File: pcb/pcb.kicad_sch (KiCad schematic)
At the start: 21 parts, among them J1 USB_C_Receptacle_USB2.0_14P, U1 RP2040, U2 NCP1117-3.3_SOT223

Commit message: logging off for the night - completed the schematic
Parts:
- added C15, C16: 33pF, Capacitor_SMD:C_0402_1005Metric, symbol Device:C
- added C17: 0.1uF, Capacitor_SMD:C_0402_1005Metric, symbol Device:C
- added J2, J3: Conn_01x20, Connector_PinHeader_2.54mm:PinHeader_1x20_P2.54mm_Vertical, symbol Connector_Generic:Conn_01x20
- added J4: Conn_01x03, Connector_PinHeader_2.54mm:PinHeader_1x03_P2.54mm_Vertical, symbol Connector_Generic:Conn_01x03
- added R5, R6: 1k, Resistor_SMD:R_0402_1005Metric, symbol Device:R
- added R7: 10k, Resistor_SMD:R_0402_1005Metric, symbol Device:R
- added SW1: SW_Push, Button_Switch_SMD:SW_Push_SPST_NO_Alps_SKRK, symbol Switch:SW_Push
- added U3: W25Q128JVS, Package_SO:SOIC-8_5.3x5.3mm_P1.27mm, symbol Memory_Flash:W25Q128JVS
- added Y1: 12 MHz, Crystal:Crystal_SMD_3225-4Pin_3.2x2.5mm, symbol Device:Crystal_GND24
- C1, C10, C11, C12, C13, C14, C2, C3, C4, C5, C6, C7, C8, C9: footprint (none) -> Capacitor_SMD:C_0402_1005Metric
- J1: footprint (none) -> Connector_USB:USB_C_Receptacle_HRO_TYPE-C-31-M-12
- R1, R2, R3, R4: footprint (none) -> Resistor_SMD:R_0402_1005Metric
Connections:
- net +3V3: now also C17.1, J3.5 (Pin_5), R7.1, U3.8 (VCC)
- net GND: now also U1.19 (TESTEN), C15.1, C16.1, C17.2, J2.13 (Pin_13), J2.18 (Pin_18), J2.3 (Pin_3), J2.8 (Pin_8), J3.13 (Pin_13), J3.18 (Pin_18), J3.3 (Pin_3), J3.8 (Pin_8), J4.2 (Pin_2), SW1.1, U3.4 (GND), Y1.2, Y1.4
- net VBUS: now also J3.1 (Pin_1)
- net GPIO8: now reaches U1.11 (GPIO8)
- net GPIO8: now also J2.11 (Pin_11)
- net GPIO9: now reaches U1.12 (GPIO9)
- net GPIO9: now also J2.12 (Pin_12)
- net GPIO10: now reaches U1.13 (GPIO10)
- net GPIO10: now also J2.14 (Pin_14)
- net GPIO11: now reaches U1.14 (GPIO11)
- net GPIO11: now also J2.15 (Pin_15)
- net GPIO12: now reaches U1.15 (GPIO12)
- net GPIO12: now also J2.16 (Pin_16)
- net GPIO13: now reaches U1.16 (GPIO13)
- net GPIO13: now also J2.17 (Pin_17)
- net GPIO14: now reaches U1.17 (GPIO14)
- net GPIO14: now also J2.19 (Pin_19)
- net GPIO15: now reaches U1.18 (GPIO15)
- net GPIO15: now also J2.20 (Pin_20)
- net GPIO0: now reaches U1.2 (GPIO0)
- net GPIO0: now also J2.1 (Pin_1)
- net XIN: now reaches U1.20 (XIN)
- net XIN: now also C16.2, Y1.3
- net XOUT: now reaches U1.21 (XOUT)
- net XOUT: now also R5.2
- net SWCLK: now reaches U1.24 (SWCLK)
- net SWCLK: now also J4.1 (Pin_1)
- net SWD: now reaches U1.25 (SWD)
- net SWD: now also J4.3 (Pin_3)
- net RUN: now reaches U1.26 (RUN)
- net RUN: now also J3.11 (Pin_11)
- net GPIO16: now reaches U1.27 (GPIO16)
- net GPIO16: now also J3.20 (Pin_20)
- net GPIO17: now reaches U1.28 (GPIO17)
- net GPIO17: now also J3.19 (Pin_19)
- net GPIO18: now reaches U1.29 (GPIO18)
- net GPIO18: now also J3.17 (Pin_17)
- net GPIO1: now reaches U1.3 (GPIO1)
- net GPIO1: now also J2.2 (Pin_2)
- net GPIO19: now reaches U1.30 (GPIO19)
- net GPIO19: now also J3.16 (Pin_16)
- net GPIO20: now reaches U1.31 (GPIO20)
- net GPIO20: now also J3.15 (Pin_15)
- net GPIO21: now reaches U1.32 (GPIO21)
- net GPIO21: now also J3.14 (Pin_14)
- net GPIO22: now reaches U1.34 (GPIO22)
- net GPIO22: now also J3.12 (Pin_12)
- net GPIO23: now reaches U1.35 (GPIO23)
- net GPIO23: now also J3.10 (Pin_10)
- net GPIO24: now reaches U1.36 (GPIO24)
- net GPIO24: now also J3.9 (Pin_9)
- net GPIO26_ADC0: now reaches U1.38 (GPIO26_ADC0)
- net GPIO26_ADC0: now also J3.7 (Pin_7)
- net GPIO27_ADC1: now reaches U1.39 (GPIO27_ADC1)
- net GPIO27_ADC1: now also J3.6 (Pin_6)
- net GPIO2: now reaches U1.4 (GPIO2)
- net GPIO2: now also J2.4 (Pin_4)
- net GPIO28_ADC2: now reaches U1.40 (GPIO28_ADC2)
- net GPIO28_ADC2: now also J3.4 (Pin_4)
- net GPIO29_ADC3: now reaches U1.41 (GPIO29_ADC3)
- net GPIO29_ADC3: now also J3.2 (Pin_2)
- net GPIO3: now reaches U1.5 (GPIO3)
- net GPIO3: now also J2.5 (Pin_5)
- net QSPI_SD3: now reaches U1.51 (QSPI_SD3)
- net QSPI_SD3: now also U3.7 (~{HOLD}/~{RESET}/IO_{3})
- net QSPI_SCLK: now reaches U1.52 (QSPI_SCLK)
- net QSPI_SCLK: now also U3.6 (CLK)
- net QSPI_SD0: now reaches U1.53 (QSPI_SD0)
- net QSPI_SD0: now also U3.5 (DI/IO_{0})
- net QSPI_SD2: now reaches U1.54 (QSPI_SD2)
- net QSPI_SD2: now also U3.3 (~{WP}/IO_{2})
- net QSPI_SD1: now reaches U1.55 (QSPI_SD1)
- net QSPI_SD1: now also U3.2 (DO/IO_{1})
- net QSPI_SS: now reaches U1.56 (QSPI_SS)
- net QSPI_SS: now also R6.2, R7.2, U3.1 (~{CS})
- net GPIO4: now reaches U1.6 (GPIO4)
- net GPIO4: now also J2.6 (Pin_6)
- net GPIO5: now reaches U1.7 (GPIO5)
- net GPIO5: now also J2.7 (Pin_7)
- net GPIO6: now reaches U1.8 (GPIO6)
- net GPIO6: now also J2.9 (Pin_9)
- net GPIO7: now reaches U1.9 (GPIO7)
- net GPIO7: now also J2.10 (Pin_10)
- new net: R6.1, SW1.2
- new net: C15.2, R5.1, Y1.1
- no-connect marks 0 -> 1
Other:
- moved on the sheet: C1, C13, C14, C2, C3, C4, C5, C6, C7, C8, C9, J1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

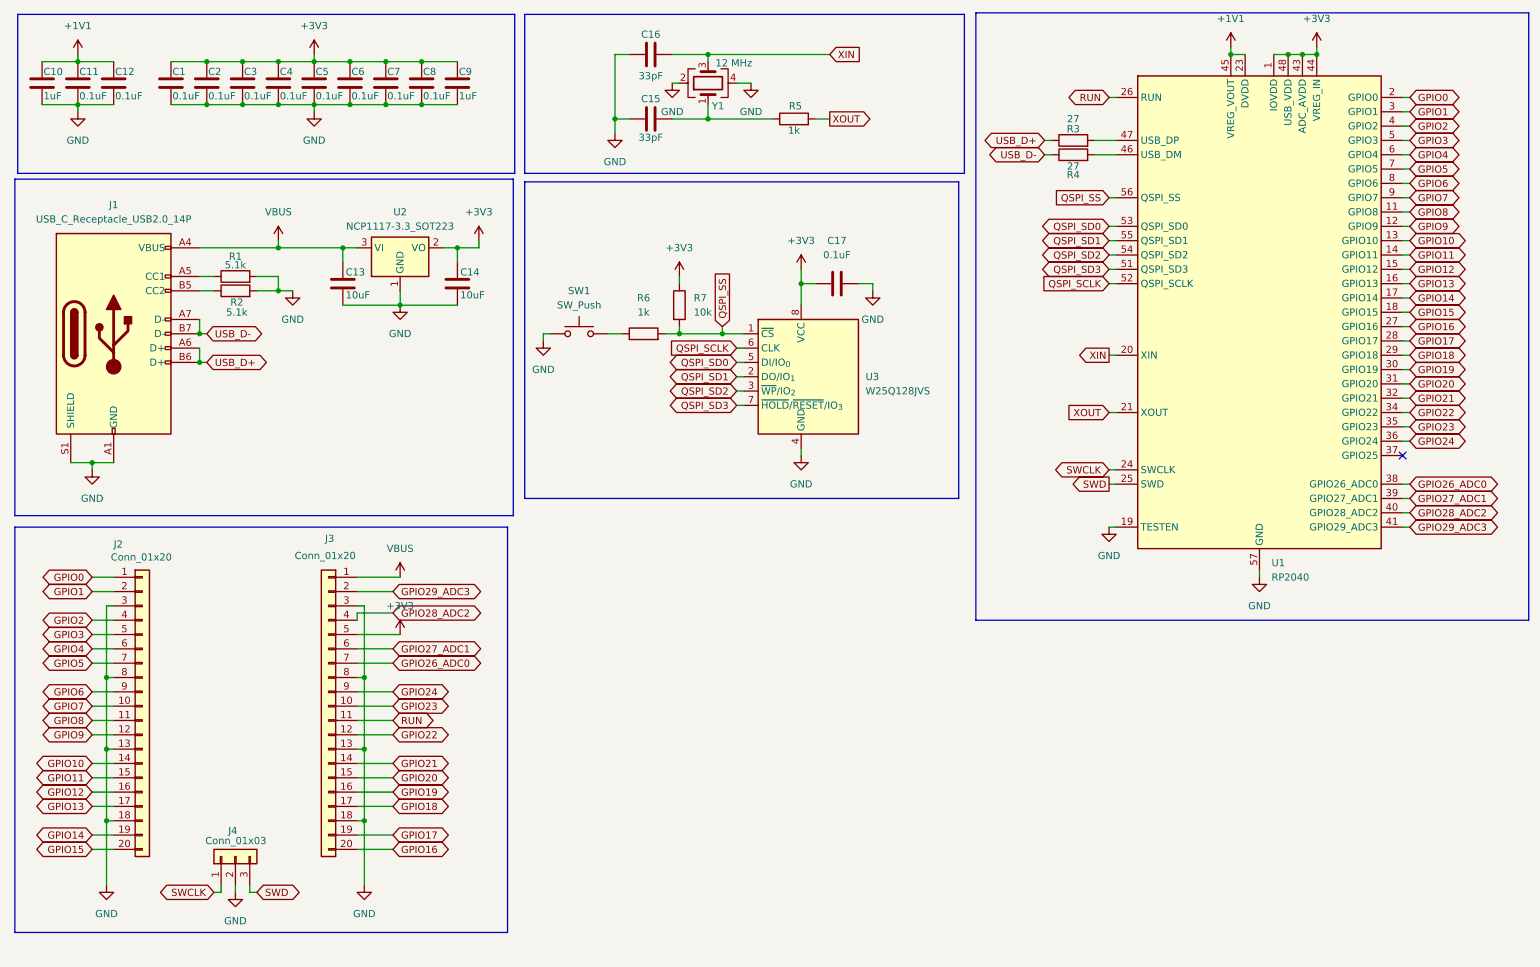
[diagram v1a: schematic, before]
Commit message: feat: added the neopixel status led
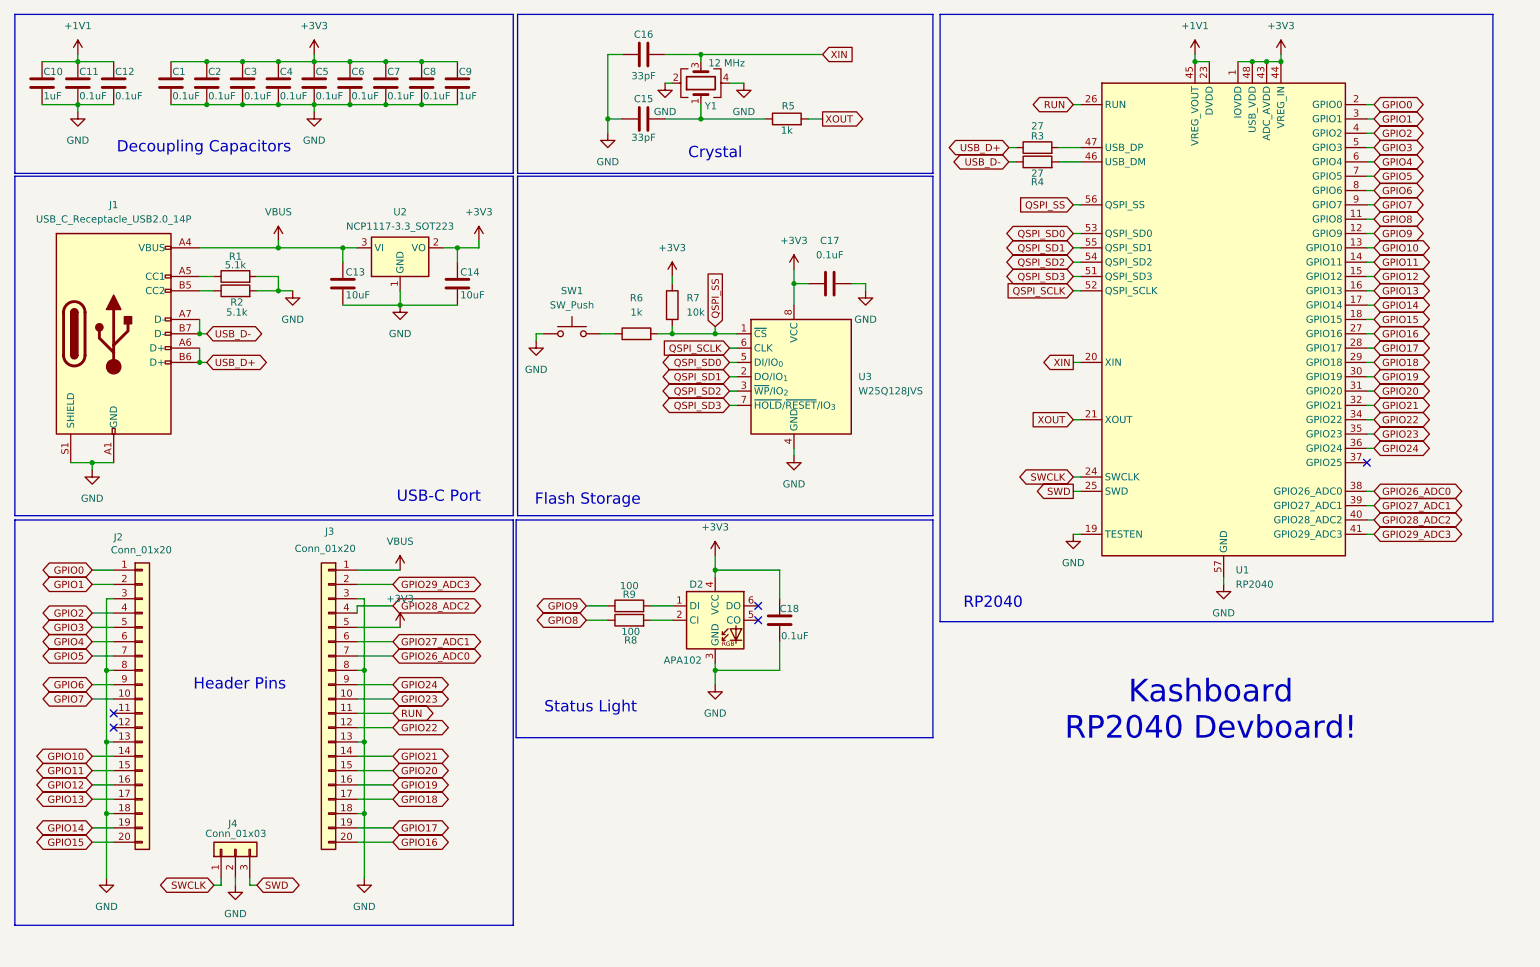
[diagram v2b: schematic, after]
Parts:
- added C18: 0.1uF, symbol Device:C
- added D2: APA102, LED_SMD:LED_RGB_5050-6, symbol LED:APA102
- added R8, R9: 100, symbol Device:R
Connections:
- net +3V3: now also C18.1, D2.4 (VCC)
- net GND: now also C18.2, D2.3 (GND)
- net GPIO8: now also R8.1; no longer J2.11 (Pin_11)
- net GPIO9: now also R9.1; no longer J2.12 (Pin_12)
- new net: D2.1 (DI), R9.2
- new net: D2.2 (CI), R8.2
- no-connect marks 1 -> 5
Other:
- note added: "Crystal"
- note added: "Decoupling Capacitors"
- note added: "Flash Storage"
- note added: "Header Pins"
- note added: "Kashboard RP2040 Devboard!"
- note added: "RP2040"
- note added: "Status Light"
- note added: "USB-C Port"
- moved on the sheet: C15, C16, C17, J2, J3, J4, R3, R4, R5, R6, R7, SW1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

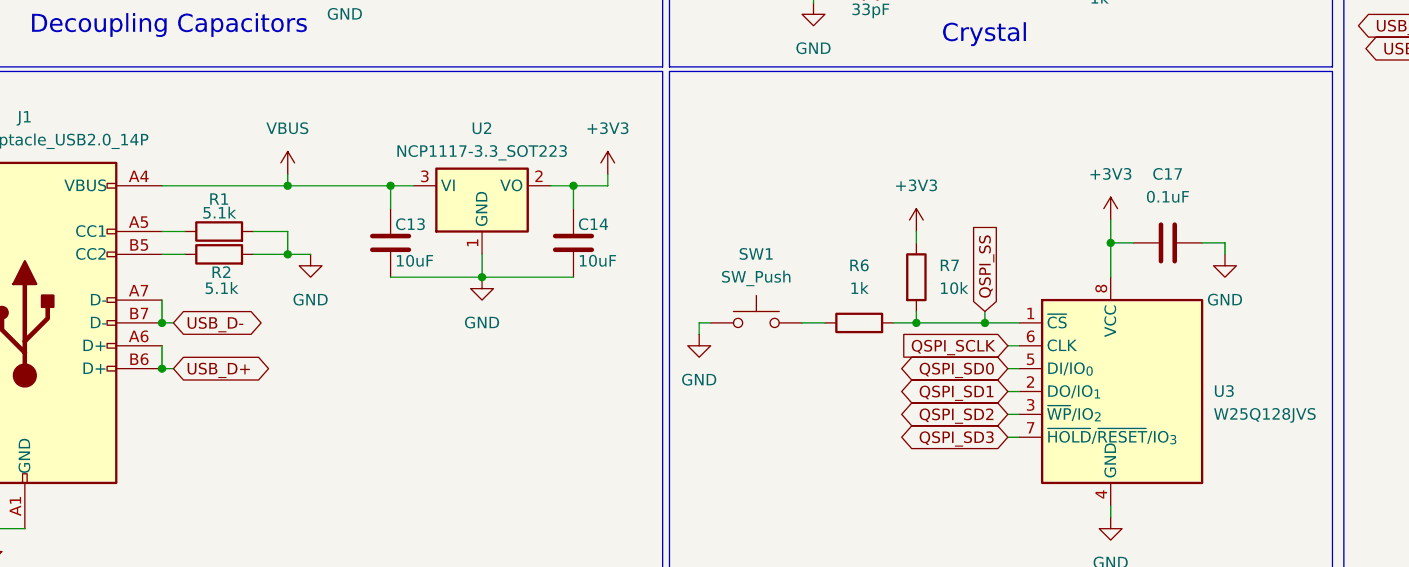
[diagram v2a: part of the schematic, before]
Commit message: updated the schematic with better formatting
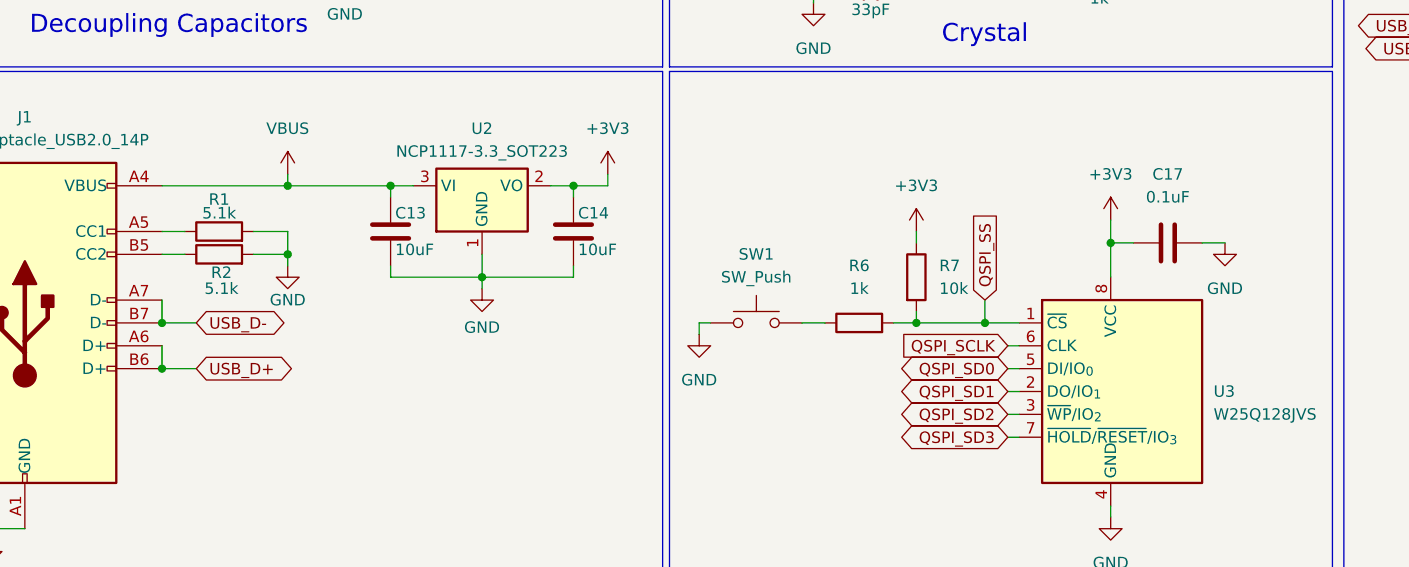
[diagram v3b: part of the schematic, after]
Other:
- moved on the sheet: C13, C14
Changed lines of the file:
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@@
 	(wire
 		(pts
-			(xy 165.1 62.23) (xy 165.1 63.5)
-		)
-		(stroke
-			(width 0)
-			(type default)
-		)
-	)
-	(wire
-		(pts
 			(xy 254 63.5) (xy 255.27 63.5)
 		)
@@
 	(wire
 		(pts
+			(xy 82.55 63.5) (xy 82.55 66.04)
+		)
+		(stroke
+			(width 0)
+			(type default)
+		)
+	)
+	(wire
+		(pts
 			(xy 73.66 30.48) (xy 80.01 30.48)
 		)
@@
 	(wire
 		(pts
-			(xy 72.39 55.88) (xy 72.39 58.42)
+			(xy 72.39 55.88) (xy 72.39 57.15)
 		)
 		(stroke
@@
 	(wire
 		(pts
-			(xy 138.43 69.85) (xy 138.43 71.12)
+			(xy 138.43 68.58) (xy 138.43 71.12)
 		)
 		(stroke
@@
 	(wire
 		(pts
-			(xy 46.99 71.12) (xy 48.26 71.12)
+			(xy 46.99 71.12) (xy 50.8 71.12)
 		)
 		(stroke
@@
 	(wire
 		(pts
-			(xy 82.55 63.5) (xy 82.55 66.04)
+			(xy 201.93 76.2) (xy 203.2 76.2)
 		)
 		(stroke
@@
 	(wire
 		(pts
-			(xy 201.93 76.2) (xy 203.2 76.2)
+			(xy 80.01 30.48) (xy 86.36 30.48)
 		)
 		(stroke
@@
 	(wire
 		(pts
-			(xy 80.01 30.48) (xy 86.36 30.48)
+			(xy 254 43.18) (xy 255.27 43.18)
 		)
 		(stroke
@@
 	(wire
 		(pts
-			(xy 254 43.18) (xy 255.27 43.18)
+			(xy 72.39 66.04) (xy 72.39 64.77)
 		)
 		(stroke
@@
 	(wire
 		(pts
-			(xy 60.96 63.5) (xy 63.5 63.5)
-		)
-		(stroke
-			(width 0)
-			(type default)
-		)
-	)
-	(wire
-		(pts
 			(xy 199.39 38.1) (xy 203.2 38.1)
 		)
@@
 	(wire
 		(pts
-			(xy 92.71 55.88) (xy 92.71 58.42)
+			(xy 92.71 55.88) (xy 92.71 57.15)
 		)
 		(stroke
@@
 	(wire
 		(pts
-			(xy 46.99 76.2) (xy 48.26 76.2)
+			(xy 46.99 76.2) (xy 50.8 76.2)
 		)
 		(stroke
@@
 	(wire
 		(pts
+			(xy 92.71 66.04) (xy 92.71 64.77)
+		)
+		(stroke
+			(width 0)
+			(type default)
+		)
+	)
+	(wire
+		(pts
 			(xy 135.89 21.59) (xy 135.89 22.86)
 		)
@@
 	(wire
 		(pts
+			(xy 60.96 64.77) (xy 60.96 63.5)
+		)
+		(stroke
+			(width 0)
+			(type default)
+		)
+	)
+	(wire
+		(pts
 			(xy 201.93 99.06) (xy 203.2 99.06)
 		)
@@
 	(wire
 		(pts
+			(xy 82.55 67.31) (xy 82.55 66.04)
+		)
+		(stroke
+			(width 0)
+			(type default)
+		)
+	)
+	(wire
+		(pts
 			(xy 27.94 158.75) (xy 31.75 158.75)
 		)
@@
 	(global_label "QSPI_SS"
 		(shape input)
-		(at 138.43 69.85 90)
+		(at 138.43 68.58 90)
 		(fields_autoplaced yes)
 		(effects
@@
 		)
 		(property "Intersheetrefs" "${INTERSHEET_REFS}"
-			(at 138.43 59.0634 90)
+			(at 138.43 57.7934 90)
 			(effects
 				(font
@@
 	(global_label "USB_D-"
 		(shape bidirectional)
-		(at 48.26 71.12 0)
+		(at 50.8 71.12 0)
 		(fields_autoplaced yes)
 		(effects
@@
 		)
 		(property "Intersheetrefs" "${INTERSHEET_REFS}"
-			(at 59.9765 71.12 0)
+			(at 62.5165 71.12 0)
 			(effects
 				(font
@@
 	(global_label "USB_D+"
 		(shape bidirectional)
-		(at 48.26 76.2 0)
+		(at 50.8 76.2 0)
 		(fields_autoplaced yes)
 		(effects
@@
 		)
 		(property "Intersheetrefs" "${INTERSHEET_REFS}"
-			(at 59.9765 76.2 0)
+			(at 62.5165 76.2 0)
 			(effects
 				(font
@@
 	(symbol
 		(lib_id "Device:C")
-		(at 72.39 62.23 180)
+		(at 72.39 60.96 180)
 		(unit 1)
 		(exclude_from_sim no)
@@
 		(dnp no)
 		(property "Reference" "C13"
-			(at 72.898 60.198 0)
+			(at 72.898 58.928 0)
 			(effects
 				(font
@@
 		)
 		(property "Value" "10uF"
-			(at 72.898 64.262 0)
+			(at 72.898 62.992 0)
 			(effects
 				(font
@@
 		)
 		(property "Footprint" "Capacitor_SMD:C_0402_1005Metric"
-			(at 71.4248 58.42 0)
+			(at 71.4248 57.15 0)
 			(effects
 				(font
@@
 		)
 		(property "Datasheet" "~"
-			(at 72.39 62.23 0)
+			(at 72.39 60.96 0)
 			(effects
 				(font
@@
 		)
 		(property "Description" "Unpolarized capacitor"
-			(at 72.39 62.23 0)
+			(at 72.39 60.96 0)
 			(effects
 				(font
@@
 	(symbol
 		(lib_id "power:GND")
-		(at 165.1 63.5 0)
+		(at 165.1 62.23 0)
 		(unit 1)
 		(exclude_from_sim no)
@@
 		(fields_autoplaced yes)
 		(property "Reference" "#PWR018"
-			(at 165.1 69.85 0)
+			(at 165.1 68.58 0)
 			(effects
 				(font
@@
 		)
 		(property "Value" "GND"
-			(at 165.1 68.58 0)
+			(at 165.1 67.31 0)
 			(effects
 				(font
@@
 		)
 		(property "Footprint" ""
-			(at 165.1 63.5 0)
+			(at 165.1 62.23 0)
 			(effects
 				(font
@@
 		)
 		(property "Datasheet" ""
-			(at 165.1 63.5 0)
+			(at 165.1 62.23 0)
 			(effects
 				(font
@@
 		)
 		(property "Description" "Power symbol creates a global label with name \"GND\" , ground"
-			(at 165.1 63.5 0)
+			(at 165.1 62.23 0)
 			(effects
 				(font
@@
 	(symbol
 		(lib_id "Device:C")
-		(at 92.71 62.23 180)
+		(at 92.71 60.96 180)
 		(unit 1)
 		(exclude_from_sim no)
@@
 		(dnp no)
 		(property "Reference" "C14"
-			(at 93.218 60.198 0)
+			(at 93.218 58.928 0)
 			(effects
 				(font
@@
 		)
 		(property "Value" "10uF"
-			(at 93.218 64.262 0)
+			(at 93.218 62.992 0)
 			(effects
 				(font
@@
 		)
 		(property "Footprint" "Capacitor_SMD:C_0402_1005Metric"
-			(at 91.7448 58.42 0)
+			(at 91.7448 57.15 0)
 			(effects
 				(font
@@
 		)
 		(property "Datasheet" "~"
-			(at 92.71 62.23 0)
+			(at 92.71 60.96 0)
 			(effects
 				(font
@@
 		)
 		(property "Description" "Unpolarized capacitor"
-			(at 92.71 62.23 0)
+			(at 92.71 60.96 0)
 			(effects
 				(font
@@
 	(symbol
 		(lib_id "power:GND")
-		(at 82.55 66.04 0)
+		(at 82.55 67.31 0)
 		(unit 1)
 		(exclude_from_sim no)
@@
 		(on_board yes)
 		(dnp no)
-		(fields_autoplaced yes)
 		(property "Reference" "#PWR010"
-			(at 82.55 72.39 0)
+			(at 82.55 73.66 0)
 			(effects
 				(font
@@
 		)
 		(property "Value" "GND"
-			(at 82.55 71.12 0)
+			(at 82.55 71.628 0)
 			(effects
 				(font
@@
 		)
 		(property "Footprint" ""
-			(at 82.55 66.04 0)
+			(at 82.55 67.31 0)
 			(effects
 				(font
@@
 		)
 		(property "Datasheet" ""
-			(at 82.55 66.04 0)
+			(at 82.55 67.31 0)
 			(effects
 				(font
@@
 		)
 		(property "Description" "Power symbol creates a global label with name \"GND\" , ground"
-			(at 82.55 66.04 0)
+			(at 82.55 67.31 0)
 			(effects
 				(font
@@
 	(symbol
 		(lib_id "power:GND")
-		(at 63.5 63.5 0)
+		(at 60.96 64.77 0)
 		(unit 1)
 		(exclude_from_sim no)
@@
 		(on_board yes)
 		(dnp no)
-		(fields_autoplaced yes)
 		(property "Reference" "#PWR09"
-			(at 63.5 69.85 0)
+			(at 60.96 71.12 0)
 			(effects
 				(font
@@
 		)
 		(property "Value" "GND"
-			(at 63.5 68.58 0)
+			(at 60.96 68.58 0)
 			(effects
 				(font
@@
 		)
 		(property "Footprint" ""
-			(at 63.5 63.5 0)
+			(at 60.96 64.77 0)
 			(effects
 				(font
@@
 		)
 		(property "Datasheet" ""
-			(at 63.5 63.5 0)
+			(at 60.96 64.77 0)
 			(effects
 				(font
@@
 		)
 		(property "Description" "Power symbol creates a global label with name \"GND\" , ground"
-			(at 63.5 63.5 0)
+			(at 60.96 64.77 0)
 			(effects
 				(font

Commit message: feat: updated most of the pcb, still have some capacitors to wire
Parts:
- removed U2: NCP1117-3.3_SOT223, Package_TO_SOT_SMD:SOT-223-3_TabPin2, symbol Regulator_Linear:NCP1117-3.3_SOT223
- removed U3: W25Q128JVS, Package_SO:SOIC-8_5.3x5.3mm_P1.27mm, symbol Memory_Flash:W25Q128JVS
- added U2: MCP1700x-330xxTT, Package_TO_SOT_SMD:SOT-23, symbol Regulator_Linear:MCP1700x-330xxTT
- added U3: W25Q16JVZPIQ, Package_SON:Winbond_USON-8-1EP_3x2mm_P0.5mm_EP0.2x1.6mm, symbol W25Q16JVZPIQ:W25Q16JVZPIQ
- C1: value 0.1uF -> 1uF
- C18: footprint (none) -> Capacitor_SMD:C_0402_1005Metric
- C9: value 1uF -> 0.1uF
- R8, R9: footprint (none) -> Resistor_SMD:R_0402_1005Metric
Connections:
- net +3V3: now also C17.2, U2.2 (VO), U3.8 (VCC); no longer C17.1
- net GND: now also C17.1, U2.1 (GND), U3.4 (GND); no longer C17.2
- net QSPI_SCLK: now also U3.6 (CLK)
- net QSPI_SD0: now also U3.5 (DI(IO0))
- net QSPI_SD1: now also U3.2 (DO(IO1))
- net QSPI_SD2: now also U3.3 (~{WP}(IO2))
- net QSPI_SD3: now also U3.7 (~{HOLD}/RESET(IO3))
- net QSPI_SS: now also U3.1 (~{CS})
- net VBUS: now also U2.3 (VI)
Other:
- moved on the sheet: C17, C18, D2, R6, R7, R8, R9, SW1
